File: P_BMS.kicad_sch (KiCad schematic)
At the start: 25 parts, among them J25 Conn_01x04, J26 Conn_01x04, J27 Conn_01x04

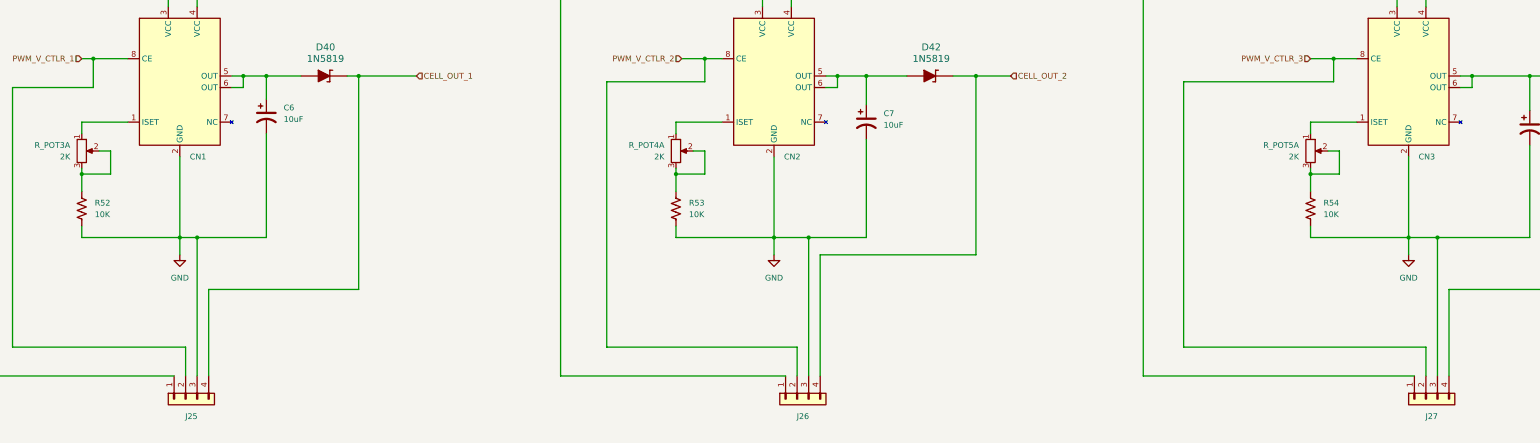
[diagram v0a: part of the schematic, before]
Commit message: PCB 90% & Corrections to diagram in the ADC section were done
Te resistors to secure a low logical level were placed, also the routing of the PCB is at the 90%
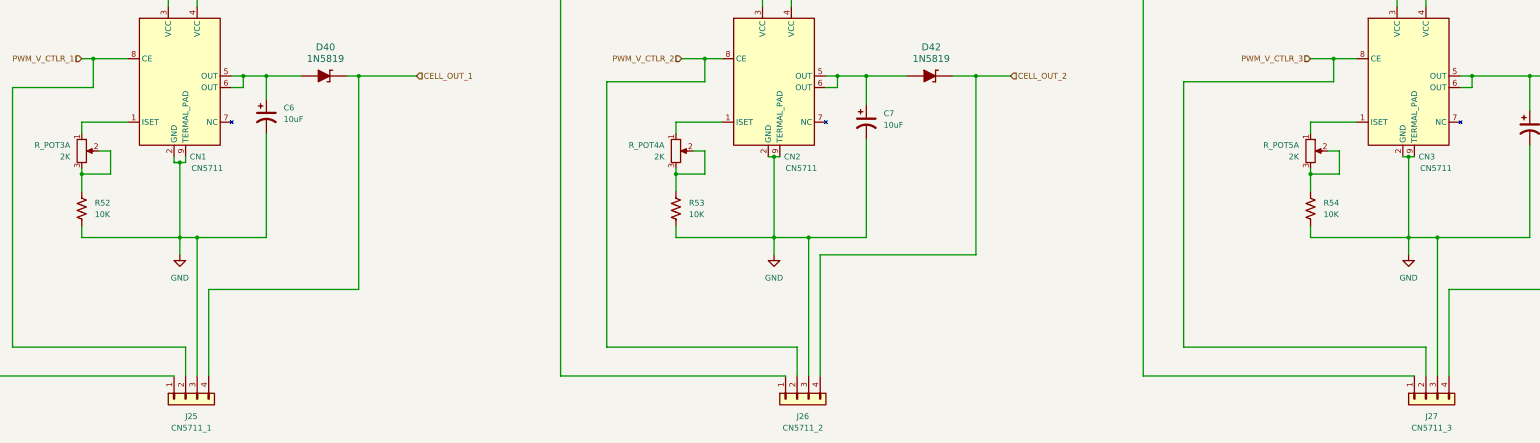
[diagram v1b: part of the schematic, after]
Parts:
- CN1, CN2, CN3: value ~ -> CN5711; footprint (none) -> Package_SO:Texas_HSOP-8-1EP_3.9x4.9mm_P1.27mm_ThermalVias
- D40, D42, D43: footprint digikey-footprints:DO-41 -> Myfoodprints:D_DO-41_SOD81_P9.20mm_Horizontal
- INA1: value ~ -> INA226; footprint (none) -> Universal_Modules:INA226 Module
- J25: value Conn_01x04 -> CN5711_1
- J26: value Conn_01x04 -> CN5711_2
- J27: value Conn_01x04 -> CN5711_3
- SHORT_1, SHORT_2: footprint TestPoint:TestPoint_Bridge_Pitch5.08mm_Drill1.3mm -> Myfoodprints:Short_5.08mm_Drill1.3mm
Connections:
- net GND: now also CN1.9 (TERMAL_PAD), CN2.9 (TERMAL_PAD), CN3.9 (TERMAL_PAD)

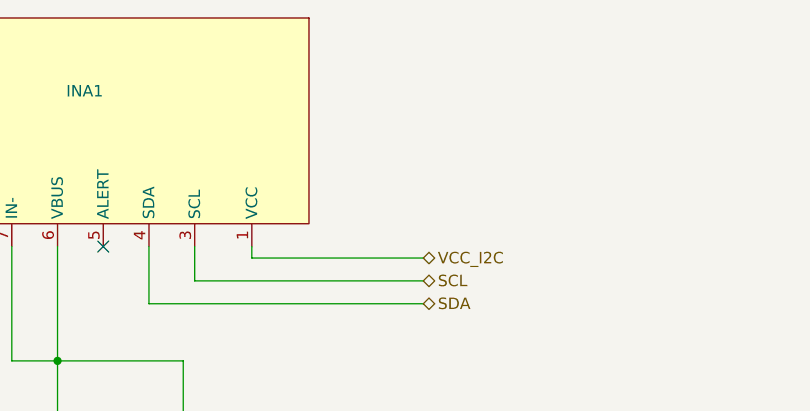
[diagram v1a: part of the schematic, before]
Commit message: Diagram updated with the pending bugfix
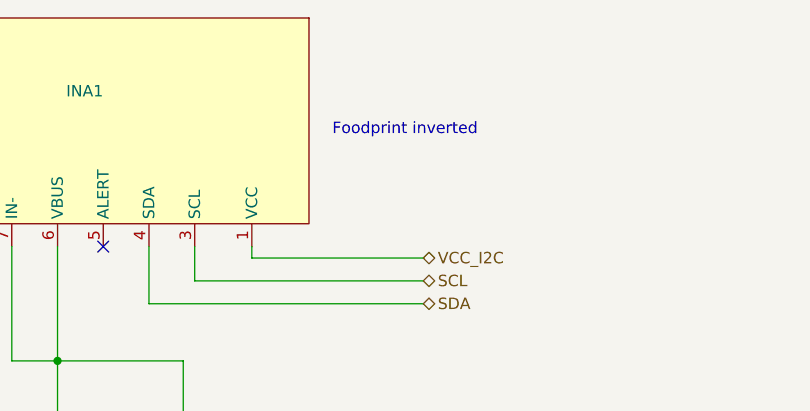
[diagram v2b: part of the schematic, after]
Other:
- note added: "Foodprint inverted"
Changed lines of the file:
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@@
+		)
+	)
+	(text "Foodprint inverted"
+		(exclude_from_sim no)
+		(at 174.498 26.416 0)
+		(effects
+			(font
+				(size 1.27 1.27)
+			)
 		)
 	)
